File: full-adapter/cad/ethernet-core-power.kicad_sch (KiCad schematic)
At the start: 16 parts, among them U13 TPS6281320QWRWYRQ1

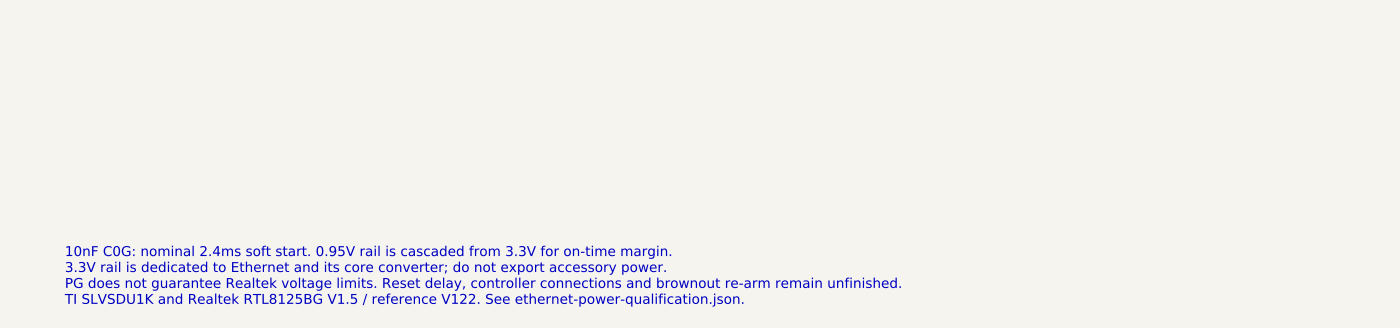
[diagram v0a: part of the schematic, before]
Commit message: Capture RTL8125BG controller clock and PCIe lanes
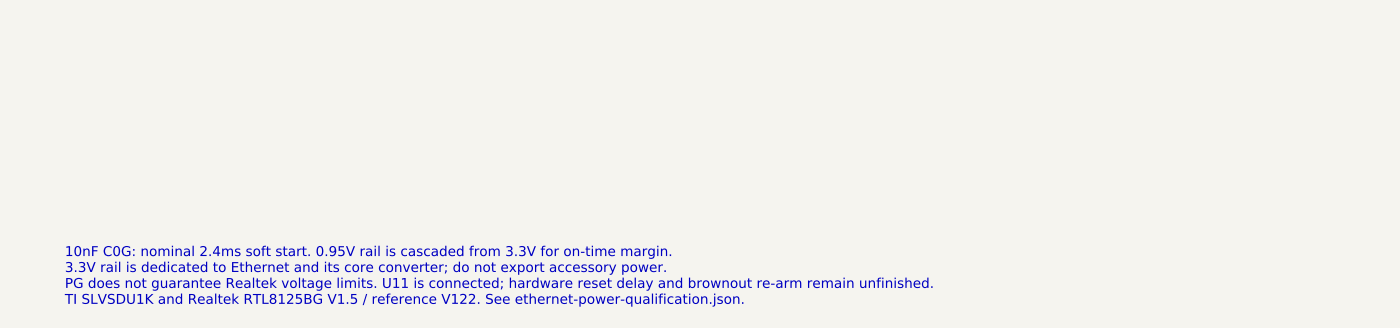
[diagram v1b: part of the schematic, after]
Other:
- note added: "10nF C0G: nominal 2.4ms soft start. 0.95V rail is cascaded from 3.3V for on-time margin. 3.3V rail is dedicated to Ethernet and its core converter; do not export accessory power. PG does not guarantee Realtek voltage limits. U11 is connected; hardware reset delay and brownout re-arm remain unfinished. TI SLVSDU1K and Realtek RTL8125BG V1.5 / reference V122. See ethernet-power-qualification.json."
- note removed: "10nF C0G: nominal 2.4ms soft start. 0.95V rail is cascaded from 3.3V for on-time margin. 3.3V rail is dedicated to Ethernet and its core converter; do not export accessory power. PG does not guarantee Realtek voltage limits. Reset delay, controller connections and brownout re-arm remain unfinished. TI SLVSDU1K and Realtek RTL8125BG V1.5 / reference V122. See ethernet-power-qualification.json."
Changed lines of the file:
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@@
 (pin "1")(instances (project "full-adapter" (path "/fda20879-fa66-56c0-be14-de2506349b46/b601bc75-3428-58e7-b8ec-bd857ea61508" (reference "#PWRethernetcorepower011") (unit 1)))))
 (text "VIN, MODE and EN crossings have no junction: EN must remain separate from VIN.\nPlace both input capacitors at VIN/GND; use compact SW/inductor copper.\nKeep five output capacitors at the regulator. Route FB as a quiet Kelvin trace.\nMODE = VIN forces PWM. FSET = GND selects 2.25MHz and compensation1." (at 15.24 213.36 0) (effects (font (size 1.27 1.27)) (justify left top)))
-(text "10nF C0G: nominal 2.4ms soft start. 0.95V rail is cascaded from 3.3V for on-time margin.\n3.3V rail is dedicated to Ethernet and its core converter; do not export accessory power.\nPG does not guarantee Realtek voltage limits. Reset delay, controller connections and brownout re-arm remain unfinished.\nTI SLVSDU1K and Realtek RTL8125BG V1.5 / reference V122. See ethernet-power-qualification.json." (at 15.24 251.46 0) (effects (font (size 1.1 1.1)) (justify left top)))
+(text "10nF C0G: nominal 2.4ms soft start. 0.95V rail is cascaded from 3.3V for on-time margin.\n3.3V rail is dedicated to Ethernet and its core converter; do not export accessory power.\nPG does not guarantee Realtek voltage limits. U11 is connected; hardware reset delay and brownout re-arm remain unfinished.\nTI SLVSDU1K and Realtek RTL8125BG V1.5 / reference V122. See ethernet-power-qualification.json." (at 15.24 251.46 0) (effects (font (size 1.1 1.1)) (justify left top)))
 )

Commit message: Capture PCIe control isolation and Ethernet startup reset
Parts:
- TP661: value ETH_CORE_PG -> ETH_RESET_CONDITION_N
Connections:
- net ETH_CORE_PG renamed ETH_RESET_CONDITION_N
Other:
- note added: "10nF C0G: nominal 2.4ms soft start. 0.95V rail is cascaded from 3.3V for on-time margin. 3.3V rail is dedicated to Ethernet and its core converter; do not export accessory power. PG shares the U16 reset condition bus. Startup delay is captured; fast fault timing and power-cycle re-arm remain open. TI SLVSDU1K and Realtek RTL8125BG V1.5 / reference V122. See ethernet-power-qualification.json."
- note removed: "10nF C0G: nominal 2.4ms soft start. 0.95V rail is cascaded from 3.3V for on-time margin. 3.3V rail is dedicated to Ethernet and its core converter; do not export accessory power. PG does not guarantee Realtek voltage limits. U11 is connected; hardware reset delay and brownout re-arm remain unfinished. TI SLVSDU1K and Realtek RTL8125BG V1.5 / reference V122. See ethernet-power-qualification.json."
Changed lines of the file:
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@@
 (pin "1")(instances (project "full-adapter" (path "/fda20879-fa66-56c0-be14-de2506349b46/b601bc75-3428-58e7-b8ec-bd857ea61508" (reference "#FLGeth660") (unit 1)))))
 (wire (pts (xy 175.26 114.3) (xy 180.34 114.3)) (stroke (width 0) (type default)))
-(global_label "ETH_CORE_PG" (at 180.34 114.3 0) (shape bidirectional) (effects (font (size 1.27 1.27)) (justify left)))
+(wire (pts (xy 180.34 114.3) (xy 180.34 160.02)) (stroke (width 0) (type default)))
+(global_label "ETH_RESET_CONDITION_N" (at 180.34 160.02 0) (shape bidirectional) (effects (font (size 1.27 1.27)) (justify left)))
 (symbol (lib_id "Device:R_Small_US") (at 309.88 172.72 0) (unit 1) (in_bom yes) (on_board yes) (dnp no) (property "Reference" "R663" (at 312.42 171.45 0) (effects (font (size 1.27 1.27)) (justify left)))
 (property "Value" "47kR 1%" (at 312.42 173.98999999999998 0) (effects (font (size 1.27 1.27)) (justify left)))
@@
 (pin "1")(instances (project "full-adapter" (path "/fda20879-fa66-56c0-be14-de2506349b46/b601bc75-3428-58e7-b8ec-bd857ea61508" (reference "#PWRethernetcorepower010") (unit 1)))))
 (wire (pts (xy 309.88 175.26) (xy 309.88 187.96)) (stroke (width 0) (type default)))
-(global_label "ETH_CORE_PG" (at 309.88 187.96 180) (shape bidirectional) (effects (font (size 1.27 1.27)) (justify right)))
-(symbol (lib_id "Connector:TestPoint") (at 360.68 177.8 0) (unit 1) (in_bom no) (on_board yes) (dnp no) (property "Reference" "TP661" (at 360.68 165.1 0) (effects (font (size 1.27 1.27)) (justify left))) (property "Value" "ETH_CORE_PG" (at 360.68 167.64 0) (effects (font (size 1.27 1.27)) (justify left))) (property "Footprint" "TestPoint:TestPoint_Pad_D1.0mm" (at 363.22 181.61 0) (effects (font (size 1.27 1.27)) (justify left)) (hide yes)) (property "Datasheet" "" (at 363.22 184.15 0) (effects (font (size 1.27 1.27)) (justify left)) (hide yes)) (property "Description" "test point" (at 363.22 186.69 0) (effects (font (size 1.27 1.27)) (justify left)) (hide yes)) (pin "1") (instances (project "full-adapter" (path "/fda20879-fa66-56c0-be14-de2506349b46/b601bc75-3428-58e7-b8ec-bd857ea61508" (reference "TP661") (unit 1)))))
+(global_label "ETH_RESET_CONDITION_N" (at 309.88 187.96 180) (shape bidirectional) (effects (font (size 1.27 1.27)) (justify right)))
+(symbol (lib_id "Connector:TestPoint") (at 360.68 177.8 0) (unit 1) (in_bom no) (on_board yes) (dnp no) (property "Reference" "TP661" (at 360.68 165.1 0) (effects (font (size 1.27 1.27)) (justify left))) (property "Value" "ETH_RESET_CONDITION_N" (at 360.68 167.64 0) (effects (font (size 1.27 1.27)) (justify left))) (property "Footprint" "TestPoint:TestPoint_Pad_D1.0mm" (at 363.22 181.61 0) (effects (font (size 1.27 1.27)) (justify left)) (hide yes)) (property "Datasheet" "" (at 363.22 184.15 0) (effects (font (size 1.27 1.27)) (justify left)) (hide yes)) (property "Description" "test point" (at 363.22 186.69 0) (effects (font (size 1.27 1.27)) (justify left)) (hide yes)) (pin "1") (instances (project "full-adapter" (path "/fda20879-fa66-56c0-be14-de2506349b46/b601bc75-3428-58e7-b8ec-bd857ea61508" (reference "TP661") (unit 1)))))
 (wire (pts (xy 360.68 177.8) (xy 360.68 187.96)) (stroke (width 0) (type default)))
 (wire (pts (xy 309.88 187.96) (xy 360.68 187.96)) (stroke (width 0) (type default)))
@@
 (pin "1")(instances (project "full-adapter" (path "/fda20879-fa66-56c0-be14-de2506349b46/b601bc75-3428-58e7-b8ec-bd857ea61508" (reference "#PWRethernetcorepower011") (unit 1)))))
 (text "VIN, MODE and EN crossings have no junction: EN must remain separate from VIN.\nPlace both input capacitors at VIN/GND; use compact SW/inductor copper.\nKeep five output capacitors at the regulator. Route FB as a quiet Kelvin trace.\nMODE = VIN forces PWM. FSET = GND selects 2.25MHz and compensation1." (at 15.24 213.36 0) (effects (font (size 1.27 1.27)) (justify left top)))
-(text "10nF C0G: nominal 2.4ms soft start. 0.95V rail is cascaded from 3.3V for on-time margin.\n3.3V rail is dedicated to Ethernet and its core converter; do not export accessory power.\nPG does not guarantee Realtek voltage limits. U11 is connected; hardware reset delay and brownout re-arm remain unfinished.\nTI SLVSDU1K and Realtek RTL8125BG V1.5 / reference V122. See ethernet-power-qualification.json." (at 15.24 251.46 0) (effects (font (size 1.1 1.1)) (justify left top)))
+(text "10nF C0G: nominal 2.4ms soft start. 0.95V rail is cascaded from 3.3V for on-time margin.\n3.3V rail is dedicated to Ethernet and its core converter; do not export accessory power.\nPG shares the U16 reset condition bus. Startup delay is captured; fast fault timing and power-cycle re-arm remain open.\nTI SLVSDU1K and Realtek RTL8125BG V1.5 / reference V122. See ethernet-power-qualification.json." (at 15.24 251.46 0) (effects (font (size 1.1 1.1)) (justify left top)))
 )
